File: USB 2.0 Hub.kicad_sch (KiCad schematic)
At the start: 30 parts, among them J1 USB_C_Receptacle_USB2.0, J2 USB_C_Receptacle_USB2.0, J3 USB_C_Receptacle_USB2.0, J4 USB_C_Receptacle_USB2.0, J5 USB_C_Receptacle_USB2.0, U1 SL2.1A

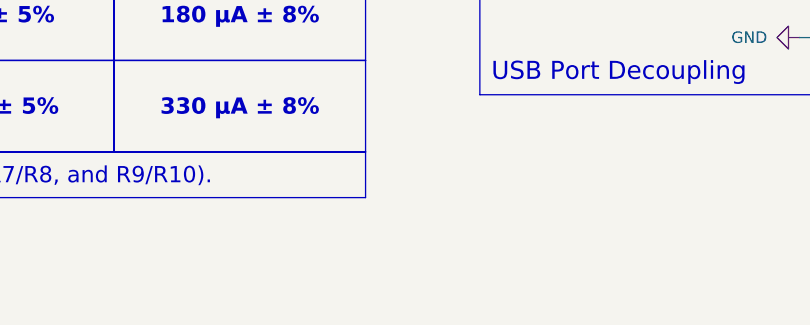
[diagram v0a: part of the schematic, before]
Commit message: Adjusting size to match wellplate
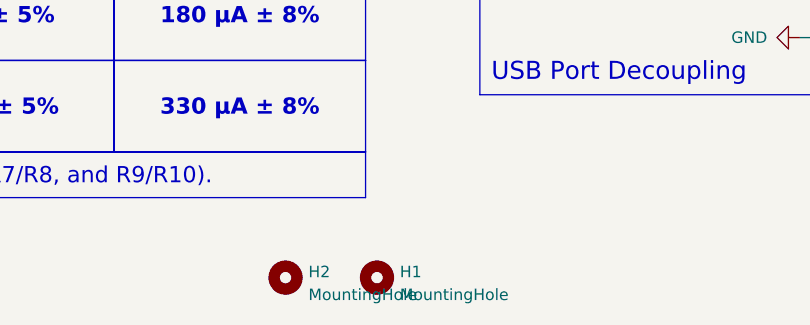
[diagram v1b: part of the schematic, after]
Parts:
- added H1, H2: MountingHole, MountingHole:MountingHole_3.2mm_M3_ISO14580, symbol Mechanical:MountingHole
- J2, J3, J4, J5: footprint Connector_USB:USB_C_Receptacle_HRO_TYPE-C-31-M-12 -> uc32_standalone_singlemotor:USB_C_Plug_UTC009-C12
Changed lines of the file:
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@@
       (effects (font (size 1.27 1.27)))
     )
-    (property "Footprint" "Connector_USB:USB_C_Receptacle_HRO_TYPE-C-31-M-12" (at 218.44 40.64 0)
+    (property "Footprint" "uc32_standalone_singlemotor:USB_C_Plug_UTC009-C12" (at 218.44 40.64 0)
       (effects (font (size 1.27 1.27)) hide)
     )
@@
       (effects (font (size 1.27 1.27)))
     )
-    (property "Footprint" "Connector_USB:USB_C_Receptacle_HRO_TYPE-C-31-M-12" (at 154.94 40.64 0)
+    (property "Footprint" "uc32_standalone_singlemotor:USB_C_Plug_UTC009-C12" (at 154.94 40.64 0)
       (effects (font (size 1.27 1.27)) hide)
     )
@@
     )
   )
+  (symbol (lib_id "Mechanical:MountingHole") (at 127 189.23 0) (unit 1)
+    (in_bom yes) (on_board yes) (dnp no) (fields_autoplaced)
+    (property "Reference" "H1" (at 129.54 188.595 0)
+      (effects (font (size 1.27 1.27)) (justify left))
+    )
+    (property "Value" "MountingHole" (at 129.54 191.135 0)
+      (effects (font (size 1.27 1.27)) (justify left))
+    )
+    (property "Footprint" "MountingHole:MountingHole_3.2mm_M3_ISO14580" (at 127 189.23 0)
+      (effects (font (size 1.27 1.27)) hide)
+    )
+    (property "Datasheet" "~" (at 127 189.23 0)
+      (effects (font (size 1.27 1.27)) hide)
+    )
+    (instances
+      (project "USB 2.0 Hub"
+        (path "/0e905e12-41c7-4c45-a4f7-d3348a506f5d"
+          (reference "H1") (unit 1)
+        )
+      )
+    )
+  )
   (symbol (lib_id "power:GND") (at 29.21 73.66 0) (unit 1)
     (in_bom yes) (on_board yes) (dnp no) (fields_autoplaced)
@@
     )
   )
+  (symbol (lib_id "Mechanical:MountingHole") (at 116.84 189.23 0) (unit 1)
+    (in_bom yes) (on_board yes) (dnp no) (fields_autoplaced)
+    (property "Reference" "H2" (at 119.38 188.595 0)
+      (effects (font (size 1.27 1.27)) (justify left))
+    )
+    (property "Value" "MountingHole" (at 119.38 191.135 0)
+      (effects (font (size 1.27 1.27)) (justify left))
+    )
+    (property "Footprint" "MountingHole:MountingHole_3.2mm_M3_ISO14580" (at 116.84 189.23 0)
+      (effects (font (size 1.27 1.27)) hide)
+    )
+    (property "Datasheet" "~" (at 116.84 189.23 0)
+      (effects (font (size 1.27 1.27)) hide)
+    )
+    (instances
+      (project "USB 2.0 Hub"
+        (path "/0e905e12-41c7-4c45-a4f7-d3348a506f5d"
+          (reference "H2") (unit 1)
+        )
+      )
+    )
+  )
   (symbol (lib_id "power:GND") (at 93.98 29.21 90) (unit 1)
     (in_bom yes) (on_board yes) (dnp no) (fields_autoplaced)
@@
       (effects (font (size 1.27 1.27)))
     )
-    (property "Footprint" "Connector_USB:USB_C_Receptacle_HRO_TYPE-C-31-M-12" (at 154.94 104.14 0)
+    (property "Footprint" "uc32_standalone_singlemotor:USB_C_Plug_UTC009-C12" (at 154.94 104.14 0)
       (effects (font (size 1.27 1.27)) hide)
     )
@@
       (effects (font (size 1.27 1.27)))
     )
-    (property "Footprint" "Connector_USB:USB_C_Receptacle_HRO_TYPE-C-31-M-12" (at 218.44 104.14 0)
-      (effects (font (size 1.27 1.27)) hide)
-    )
+    (property "Footprint" "uc32_standalone_singlemotor:USB_C_Plug_UTC009-C12" (at 218.44 104.14 0)
+      (effects (font (size 1.27 1.27)) hide)
+    )

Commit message: Swapping USB connectors
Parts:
- D1: value SD1206T020S1R0 -> RB521S30T1G; footprint Diode_SMD:D_1206_3216Metric_Pad1.42x1.75mm_HandSolder -> Diode_SMD:D_SOD-523
- J2, J3, J4, J5: footprint uc32_standalone_singlemotor:USB_C_Plug_UTC009-C12 -> Connector_USB:USB_C_Receptacle_U261-241N-4BS2SS
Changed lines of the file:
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@@
       (effects (font (size 1.27 1.27)))
     )
-    (property "Footprint" "uc32_standalone_singlemotor:USB_C_Plug_UTC009-C12" (at 218.44 40.64 0)
+    (property "Footprint" "Connector_USB:USB_C_Receptacle_U261-241N-4BS2SS" (at 218.44 40.64 0)
       (effects (font (size 1.27 1.27)) hide)
     )
@@
       (effects (font (size 1.27 1.27)))
     )
-    (property "Footprint" "uc32_standalone_singlemotor:USB_C_Plug_UTC009-C12" (at 154.94 40.64 0)
+    (property "Footprint" "Connector_USB:USB_C_Receptacle_U261-241N-4BS2SS" (at 154.94 40.64 0)
       (effects (font (size 1.27 1.27)) hide)
     )
@@
       (effects (font (size 1.27 1.27)))
     )
-    (property "Footprint" "uc32_standalone_singlemotor:USB_C_Plug_UTC009-C12" (at 154.94 104.14 0)
+    (property "Footprint" "Connector_USB:USB_C_Receptacle_U261-241N-4BS2SS" (at 154.94 104.14 0)
       (effects (font (size 1.27 1.27)) hide)
     )
@@
       (effects (font (size 1.27 1.27)))
     )
-    (property "Value" "SD1206T020S1R0" (at 59.69 25.4 0)
-      (effects (font (size 1.27 1.27)))
-    )
-    (property "Footprint" "Diode_SMD:D_1206_3216Metric_Pad1.42x1.75mm_HandSolder" (at 59.69 29.21 90)
+    (property "Value" "RB521S30T1G" (at 59.69 25.4 0)
+      (effects (font (size 1.27 1.27)))
+    )
+    (property "Footprint" "Diode_SMD:D_SOD-523" (at 59.69 29.21 90)
       (effects (font (size 1.27 1.27)) hide)
     )
@@
       (effects (font (size 1.27 1.27)))
     )
-    (property "Footprint" "uc32_standalone_singlemotor:USB_C_Plug_UTC009-C12" (at 218.44 104.14 0)
-      (effects (font (size 1.27 1.27)) hide)
-    )
+    (property "Footprint" "Connector_USB:USB_C_Receptacle_U261-241N-4BS2SS" (at 218.44 104.14 0)
+      (effects (font (size 1.27 1.27)) hide)
+    )
